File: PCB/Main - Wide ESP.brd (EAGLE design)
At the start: 73 x 61 mm, 4 parts, among them U1 ESP32DEVKITC

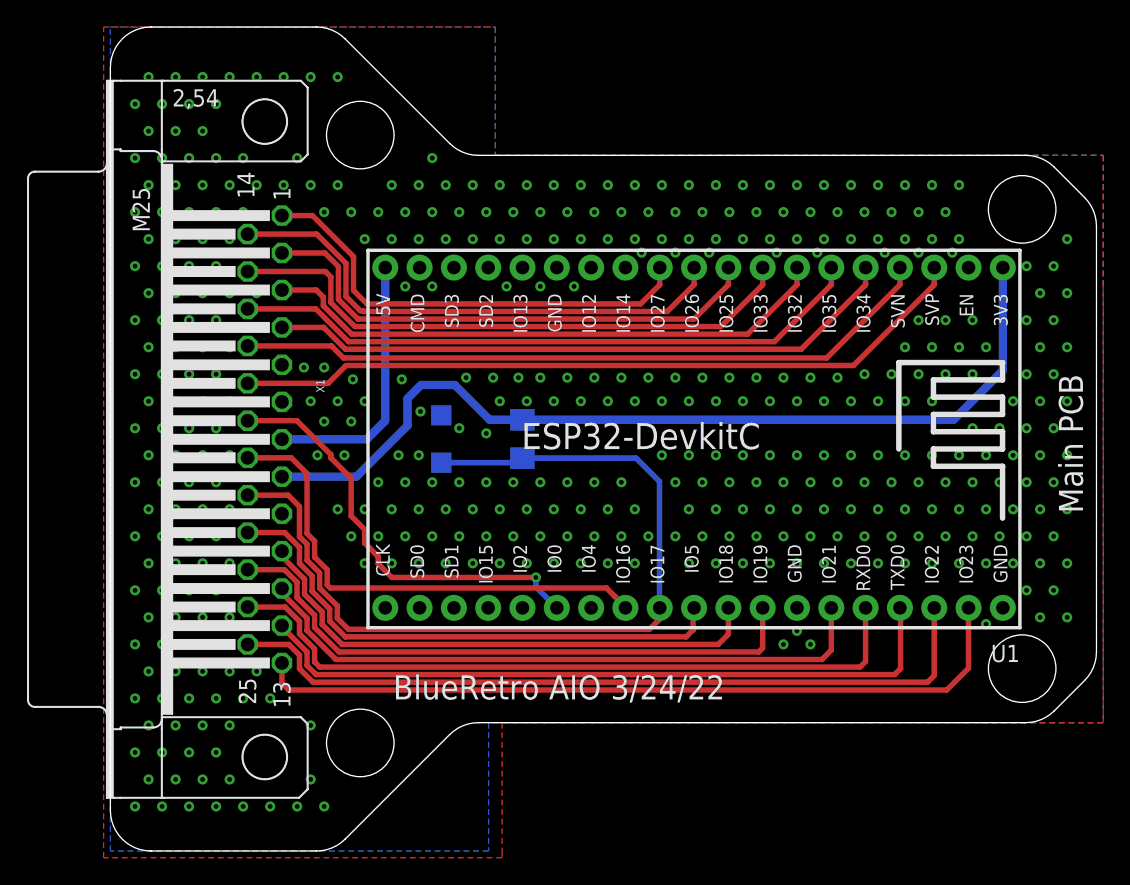
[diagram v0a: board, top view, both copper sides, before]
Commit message: Added exposed GND plane at DB25 anchors
All PCBs have been update to have exposed GND plane pads for the DB25 anchor points.

This resolves Issue 54
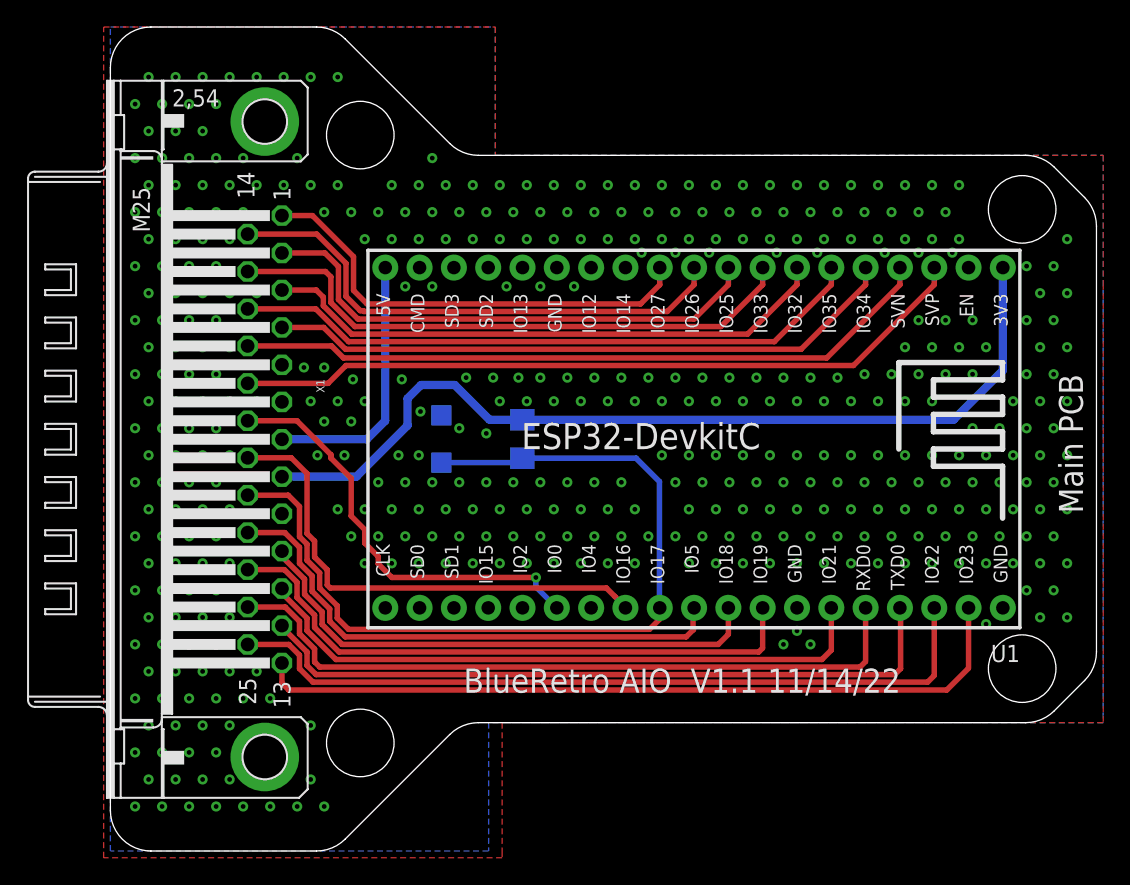
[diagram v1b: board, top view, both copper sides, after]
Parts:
- X1: device SparkFun-Retired:M25H -> SparkFun-Retired:M25HP
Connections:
- net GND: now also X1.G1, X1.G2
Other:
- board text added: "BlueRetro AIO V1.1 11/14/22"
- board text removed: "BlueRetro AIO 3/24/22"
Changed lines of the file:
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@@
 <hole x="18.5" y="8" drill="5"/>
 <text x="72" y="25" size="1.778" layer="21" rot="R90">Main PCB</text>
-<text x="45.5" y="13" size="1.778" layer="21" rot="R180">BlueRetro AIO 3/24/22</text>
+<text x="58.5" y="13.5" size="1.778" layer="21" rot="R180">BlueRetro AIO  V1.1 11/14/22</text>
 </plain>
 <attributes>
@@
 <attribute name="VALUE" x="32.913" y="31.897" size="1.27" layer="28" rot="MR270"/>
 </element>
-<element name="X1" library="SparkFun-Retired" package="M25H" value="" x="11.43" y="30.48" smashed="yes" rot="R270">
+<element name="X1" library="SparkFun-Retired" package="M25HP" value="" x="11.43" y="30.48" smashed="yes" rot="R270">
 <attribute name="NAME" x="15.24" y="34.925" size="0.6096" layer="25" font="vector" ratio="20" rot="R270"/>
 <attribute name="VALUE" x="15.24" y="29.845" size="0.6096" layer="27" font="vector" ratio="20" rot="R270"/>
@@
 <contactref element="U1" pad="38"/>
 <contactref element="U1" pad="14"/>
+<contactref element="X1" pad="G2"/>
+<contactref element="X1" pad="G1"/>
 </signal>
 <signal name="5VIN">
